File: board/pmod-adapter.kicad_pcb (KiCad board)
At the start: 2 copper layers, 20.3 x 86.4 mm, 4 parts

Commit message: Length matching.
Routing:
- net /J1A_P: track 11.2 -> 21.3 mm
- net /J1C_P: track 11.3 -> 21.2 mm
- net /J1A_N: track 11.6 -> 21.3 mm
- net /J1C_N: track 11.7 -> 21.2 mm
- net /J2A_P: track 12.1 -> 21.3 mm
- net /J2C_P: track 12.2 -> 21.2 mm
- net /J2A_N: track 12.5 -> 21.3 mm
- net /J2C_N: track 12.6 -> 21.2 mm
- net /J3A_P: track 13.0 -> 21.3 mm
- net /J3C_P: track 13.1 -> 21.2 mm
- net /J3A_N: track 13.4 -> 21.3 mm
- net /J3C_N: track 13.5 -> 21.2 mm
- net /J4C_P: track 15.8 -> 21.2 mm
- net /J4A_P: track 15.9 -> 21.3 mm
- net /J1D_P: track 16.3 -> 21.3 mm
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
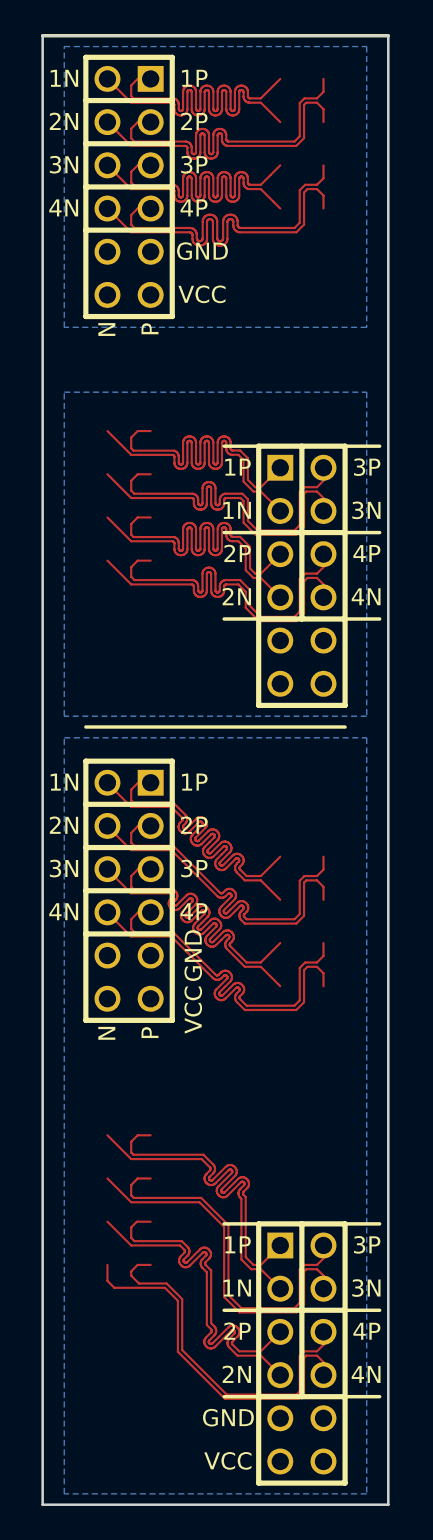
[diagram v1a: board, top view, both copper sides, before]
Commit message: Adding tie vias
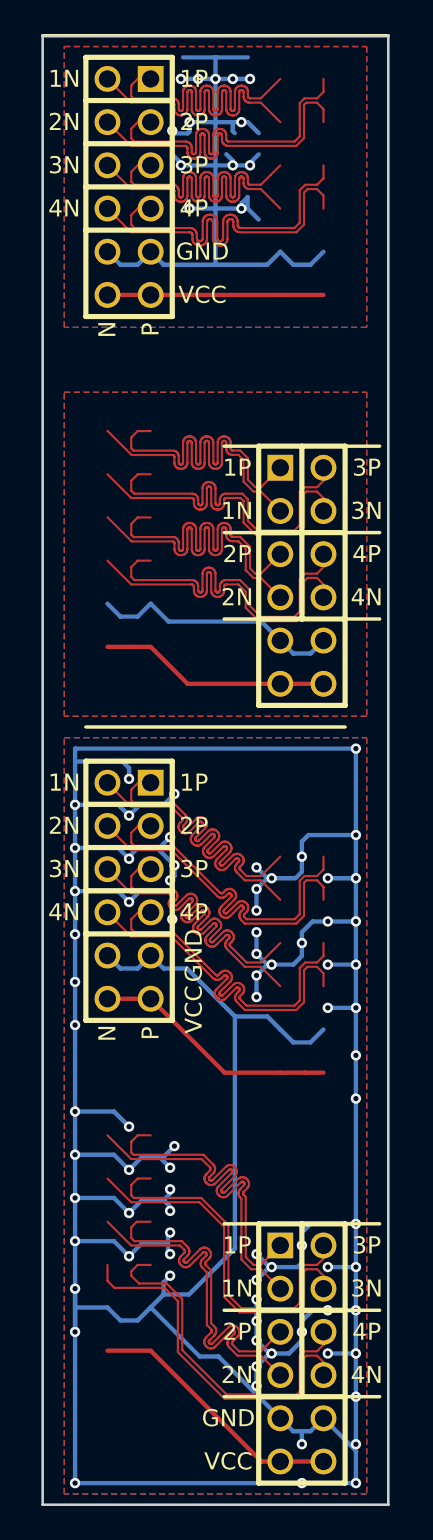
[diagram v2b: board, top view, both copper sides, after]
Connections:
- PH2 pad 12: /VCC32 -> /VCC3
- PH2 pad 6: /VCC31 -> /VCC3
- PH4 pad 12: /VCC12 -> /VCC1
- PH4 pad 6: /VCC11 -> /VCC1
- PX1 pad 12: /VCC22 -> /VCC2
- PX1 pad 6: /VCC21 -> /VCC2
- PX3 pad 12: /VCC42 -> /VCC4
- PX3 pad 6: /VCC41 -> /VCC4
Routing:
- net /GND34: track 0.00 -> 286.3 mm, vias 0 -> 79
- net /GND1: track 0.00 -> 53.4 mm, vias 0 -> 13
- net /VCC4: track 0.00 -> 15.4 mm
- net /GND2: track 0.00 -> 14.9 mm
- net /VCC3: track 0.00 -> 14.5 mm
- net /VCC2: track 0.00 -> 13.6 mm
- net /VCC1: track 0.00 -> 12.7 mm
- added copper zone on F.Cu, net /GND1
- added copper zone on F.Cu, net /GND2
- added copper zone on F.Cu, net /GND34
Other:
- net class LVDS_DP0.0254/0.0254: clearance 0.127 -> 0.126975
- rule trace_min: 0.127 -> 0.12446

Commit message: Working on the cuts and pours.
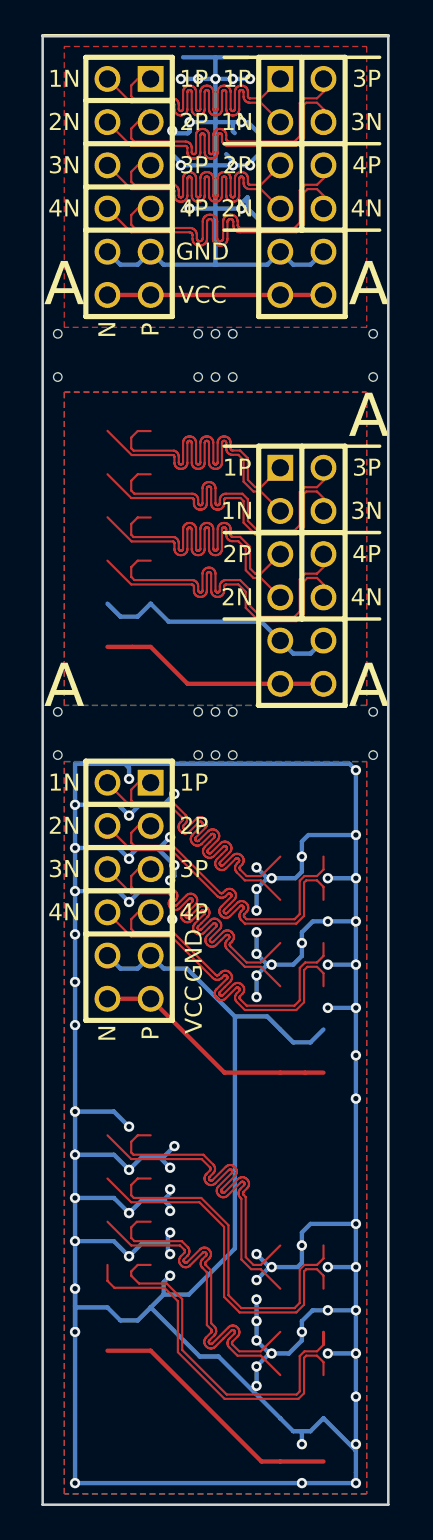
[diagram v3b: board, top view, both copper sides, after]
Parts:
- removed PH4: PMOD-Device-x2-Type-XHS, pmod-conn_6x2:pmod_pin_array_6x2_hs
- added PH1: PMOD-Device-x2-Type-XHS, pmod-conn_6x2:pmod_pin_array_6x2_hs, B.Cu at (50.8, 30.5)
- added REF**: hole, hole:smallhole, F.Cu at (46.7, 61.3)
- added REF**: hole, hole:smallhole, F.Cu at (55.0, 61.3)
- added REF**: hole, hole:smallhole, F.Cu at (55.0, 39.1)
- added REF**: hole, hole:smallhole, F.Cu at (44.7, 41.7)
- added REF**: hole, hole:smallhole, F.Cu at (45.7, 41.7)
- added REF**: hole, hole:smallhole, F.Cu at (46.7, 41.7)
- added REF**: hole, hole:smallhole, F.Cu at (36.4, 41.7)
- added REF**: hole, hole:smallhole, F.Cu at (55.0, 41.7)
- added REF**: hole, hole:smallhole, F.Cu at (36.4, 39.1)
- added REF**: hole, hole:smallhole, F.Cu at (44.7, 39.1)
- added REF**: hole, hole:smallhole, F.Cu at (45.7, 39.1)
- added REF**: hole, hole:smallhole, F.Cu at (36.4, 63.9)
- added REF**: hole, hole:smallhole, F.Cu at (46.7, 39.1)
- added REF**: hole, hole, F.Cu at (50.8, 62.6)
- added REF**: hole, hole, F.Cu at (40.6, 62.6)
- added REF**: hole, hole, F.Cu at (40.6, 40.4)
- added REF**: hole, hole, F.Cu at (50.8, 40.4)
- added REF**: hole, hole:smallhole, F.Cu at (44.7, 61.3)
- added REF**: hole, hole:smallhole, F.Cu at (36.4, 61.3)
- added REF**: hole, hole:smallhole, F.Cu at (45.7, 61.3)
- added REF**: hole, hole:smallhole, F.Cu at (45.7, 63.9)
- added REF**: hole, hole:smallhole, F.Cu at (44.7, 63.9)
- added REF**: hole, hole:smallhole, F.Cu at (46.7, 63.9)
- added REF**: hole, hole:smallhole, F.Cu at (55.0, 63.9)
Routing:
- net /GND34: track 286.3 -> 273.8 mm, vias 79 -> 73
- net (no net): track 0.00 -> 10.4 mm, vias 0 -> 6
- removed copper zone on B.Cu, net /GND1
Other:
- rule pad_to_mask_clearance: 0.2 -> 0.127
- board text added: "A"
- board text added: "B"
- board text added: "Break Line 2"
